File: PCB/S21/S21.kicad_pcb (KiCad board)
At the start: 2 copper layers, 70 x 70 mm, 32 parts, among them J1 1x5, J2 Shelly, J3 USB-PROG, J4 1x5, Q1 BSS138PS, Q2 BSS138PS, U3 MD8942, U4 ESP32-S3-MINI-1

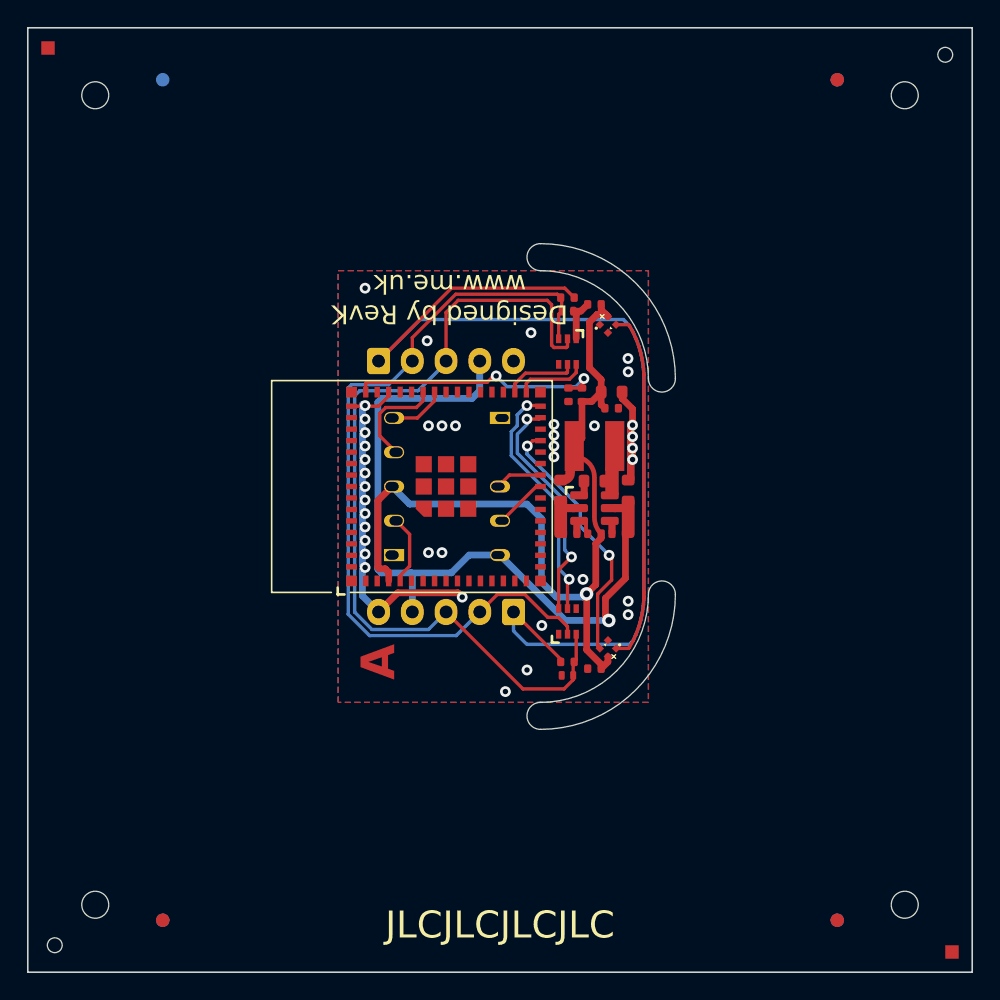
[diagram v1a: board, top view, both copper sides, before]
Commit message: Fixed render
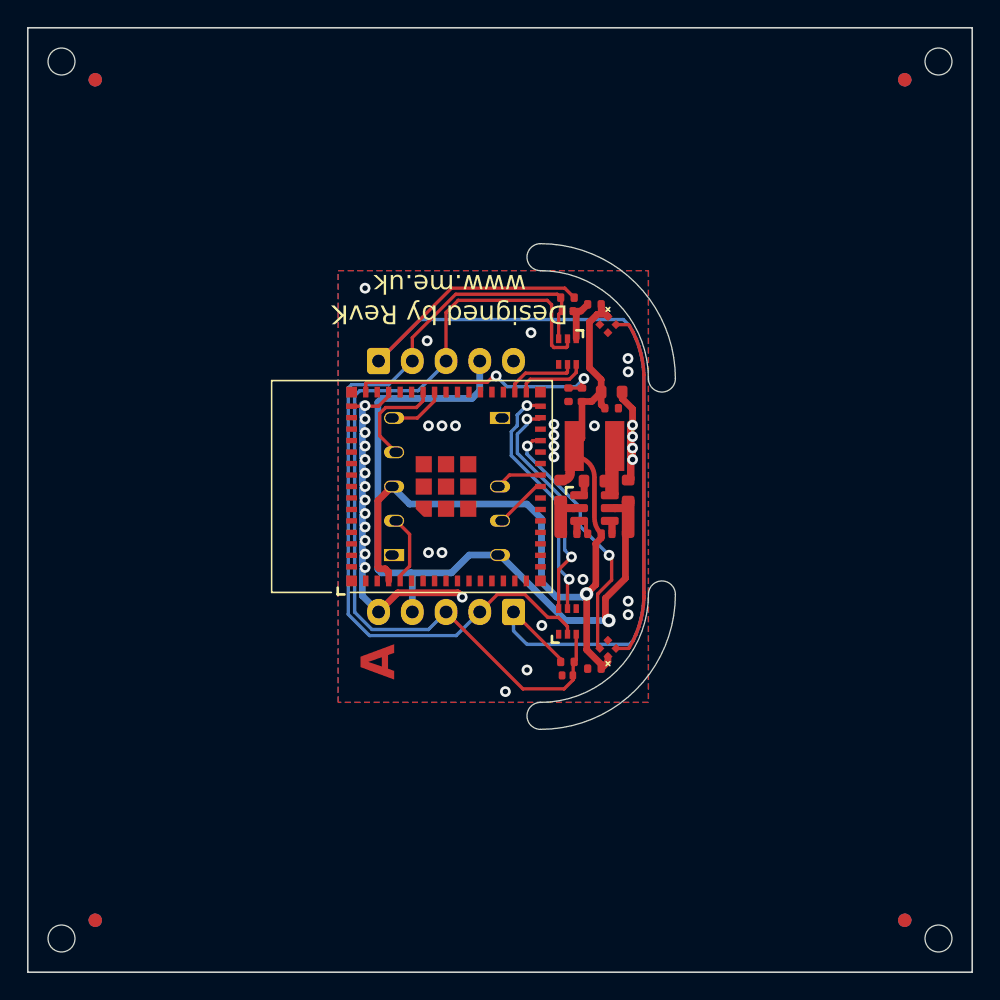
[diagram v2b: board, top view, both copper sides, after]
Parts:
- U4: value ESP32-S3-MINI-1 -> ESP32-S3-MINI-1-N4R2
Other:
- board text added: "S21-Debug"
- board text removed: "6 V-cuts"
- board text removed: "70x70mm panel"
- board text removed: "F"
- board text removed: "aikin+"
